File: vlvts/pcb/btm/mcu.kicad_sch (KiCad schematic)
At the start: 3 parts, among them J5 Conn_ARM_JTAG_SWD_10, U6 Holyiot-18010

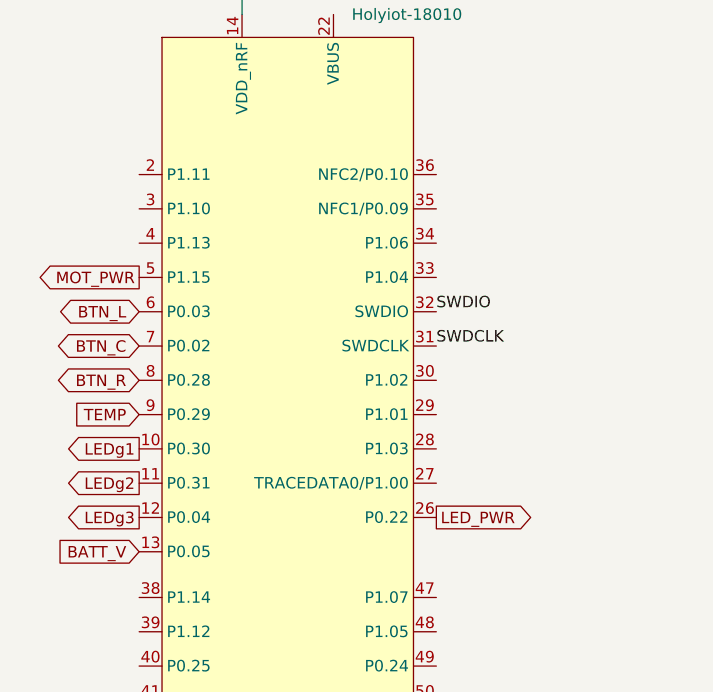
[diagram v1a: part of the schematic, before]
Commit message: vlvts: new pcb
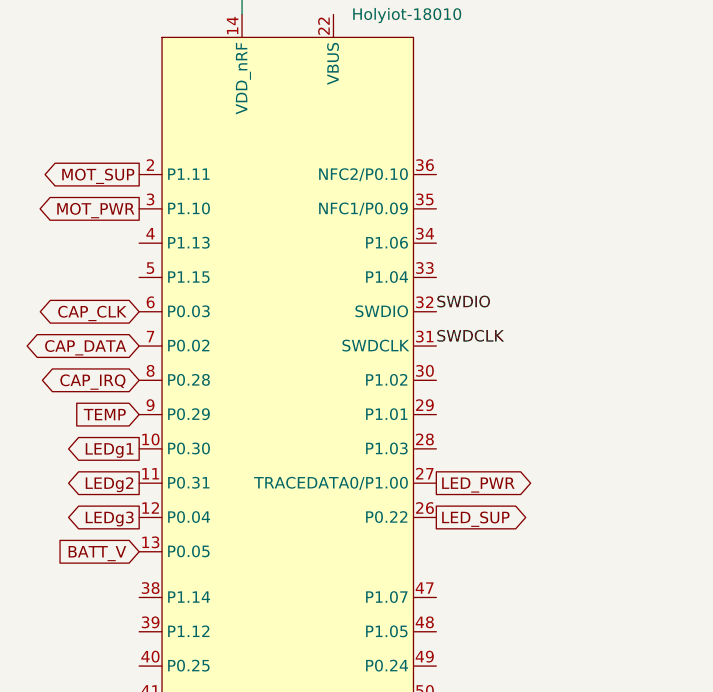
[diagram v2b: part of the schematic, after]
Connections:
- net LED_PWR: now also U6.27 (TRACEDATA0/P1.00); no longer U6.26 (P0.22)
- net MOT_PWR: now also U6.3 (P1.10); no longer U6.5 (P1.15)
- net MOT_SUP: now reaches U6.2 (P1.11)
- net BTN_C renamed CAP_DATA
- net BTN_L renamed CAP_CLK
- net BTN_R renamed CAP_IRQ
- new net LED_SUP: U6.26 (P0.22)
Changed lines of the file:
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@@
+		)
+	)
+	(global_label "LED_PWR"
+		(shape output)
+		(at 128.27 87.63 0)
+		(fields_autoplaced yes)
+		(effects
+			(font
+				(size 1.27 1.27)
+			)
+			(justify left)
+		)
+		(property "Intersheetrefs" "${INTERSHEET_REFS}"
+			(at 139.0893 87.5506 0)
+			(effects
+				(font
+					(size 1.27 1.27)
+				)
+				(justify left)
+				(hide yes)
+			)
 		)
 	)
@@
 		)
 	)
-	(global_label "LED_PWR"
+	(global_label "LED_SUP"
 		(shape output)
 		(at 128.27 91.44 0)
@@
 		)
 		(property "Intersheetrefs" "${INTERSHEET_REFS}"
-			(at 139.0893 91.3606 0)
+			(at 139.4799 91.44 0)
 			(effects
 				(font
@@
 		)
 	)
-	(global_label "MOT_PWR"
-		(shape output)
-		(at 95.25 64.77 180)
-		(fields_autoplaced yes)
-		(effects
-			(font
-				(size 1.27 1.27)
-			)
-			(justify right)
-		)
-		(property "Intersheetrefs" "${INTERSHEET_REFS}"
-			(at 84.1283 64.6906 0)
+	(global_label "MOT_SUP"
+		(shape output)
+		(at 95.25 53.34 180)
+		(fields_autoplaced yes)
+		(effects
+			(font
+				(size 1.27 1.27)
+			)
+			(justify right)
+		)
+		(property "Intersheetrefs" "${INTERSHEET_REFS}"
+			(at 83.7377 53.34 0)
 			(effects
 				(font
@@
 		)
 	)
-	(global_label "BTN_L"
+	(global_label "CAP_CLK"
 		(shape bidirectional)
 		(at 95.25 68.58 180)
@@
 		)
 		(property "Intersheetrefs" "${INTERSHEET_REFS}"
-			(at 87.2731 68.6594 0)
-			(effects
-				(font
-					(size 1.27 1.27)
-				)
-				(justify right)
-				(hide yes)
-			)
-		)
-	)
-	(global_label "BTN_R"
+			(at 82.9892 68.58 0)
+			(effects
+				(font
+					(size 1.27 1.27)
+				)
+				(justify right)
+				(hide yes)
+			)
+		)
+	)
+	(global_label "CAP_IRQ"
 		(shape bidirectional)
 		(at 95.25 76.2 180)
@@
 		)
 		(property "Intersheetrefs" "${INTERSHEET_REFS}"
-			(at 87.0312 76.2794 0)
+			(at 83.352 76.2 0)
 			(effects
 				(font
@@
 		)
 	)
-	(global_label "BTN_C"
+	(global_label "CAP_DATA"
 		(shape bidirectional)
 		(at 95.25 72.39 180)
@@
 		)
 		(property "Intersheetrefs" "${INTERSHEET_REFS}"
-			(at 87.0312 72.4694 0)
-			(effects
-				(font
+			(at 82.1425 72.39 0)
+			(effects
+				(font
+					(size 1.27 1.27)
+				)
+				(justify right)
+				(hide yes)
+			)
+		)
+	)
+	(global_label "MOT_PWR"
+		(shape output)
+		(at 95.25 57.15 180)
+		(fields_autoplaced yes)
+		(effects
+			(font
+				(size 1.27 1.27)
+			)
+			(justify right)
+		)
+		(property "Intersheetrefs" "${INTERSHEET_REFS}"
+			(at 83.5563 57.15 0)
+			(effects
+				(font
